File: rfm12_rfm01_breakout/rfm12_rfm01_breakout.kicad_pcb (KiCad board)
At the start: 2 copper layers, 32 x 24 mm, 13 parts, among them J1 ANT, J2 CONN_01X07, J3 INT, U1 RFM12B

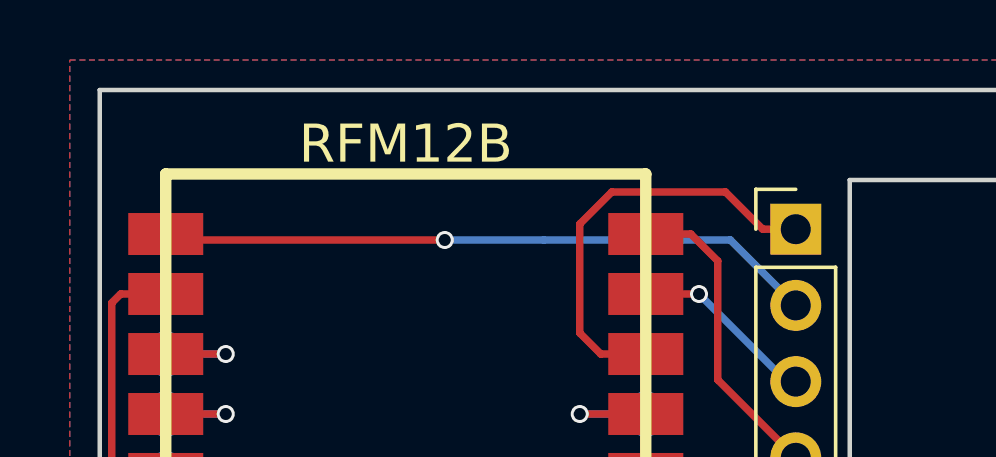
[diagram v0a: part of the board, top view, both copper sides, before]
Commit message: Minor silkscreen adjustments
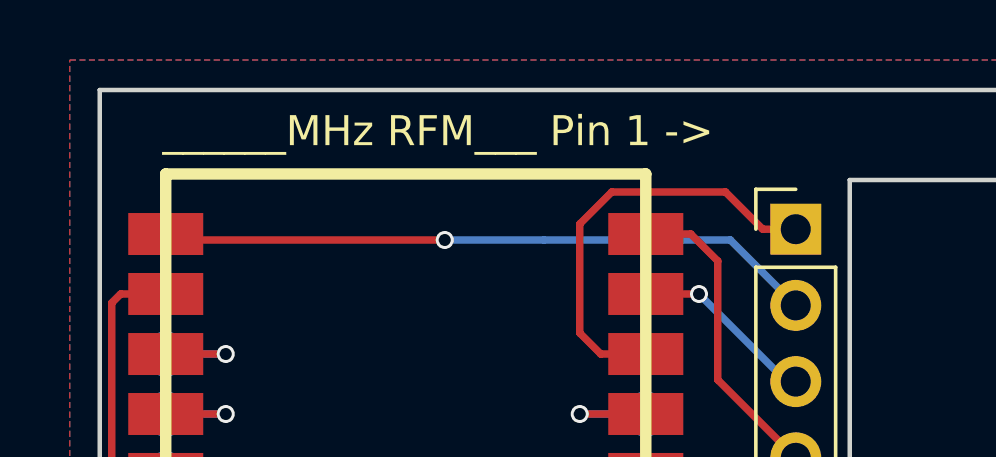
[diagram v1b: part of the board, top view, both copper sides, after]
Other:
- board text added: "For compatibility with using I2S boards at the same time, see manual in ZeroPhone Wiki"
- board text added: "RFM12/RFM01 mod board for ZeroPhone v1.0"
- board text added: "______MHz RFM___ Pin 1 ->"
- board text removed: "<- Pin 1"
- board text removed: "RFM12/RFM01 mod board for ZeroPhone For compatibility with using I2S boards at the same time, see manual in ZeroPhone Wiki"
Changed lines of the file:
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@@
-(kicad_pcb (version 4) (host pcbnew 4.0.6)
+(kicad_pcb (version 4) (host pcbnew 4.0.7)
   (general
     (links 22)
-    (no_connects 1)
+    (no_connects 0)
     (area 134.924999 98.924999 167.075001 123.075001)
     (thickness 1.6)
-    (drawings 8)
+    (drawings 9)
     (tracks 141)
     (zones 0)
@@
       (net 5 INT))
     (model ${KISYS3DMOD}/Pin_Headers.3dshapes/Pin_Header_Angled_1x07_Pitch2.54mm.wrl
-      (at (xyz 0 -0.3 0))
+      (at (xyz 0 0 0))
       (scale (xyz 1 1 1))
-      (rotate (xyz 0 0 90))
+      (rotate (xyz 0 0 0))
     )
   )
@@
       (effects (font (size 1 1) (thickness 0.15)) (justify mirror))
     )
-    (fp_text value FDF (at 1.6 0 90) (layer B.SilkS)
+    (fp_text value FDF (at -1.575 0 90) (layer B.SilkS)
       (effects (font (size 0.7 0.7) (thickness 0.15)) (justify mirror))
     )
@@
       (effects (font (size 1 1) (thickness 0.15)) (justify mirror))
     )
-    (fp_text value DCF (at -1.6 0 270) (layer B.SilkS)
+    (fp_text value DCF (at 1.525 -0.025 270) (layer B.SilkS)
       (effects (font (size 0.7 0.7) (thickness 0.15)) (justify mirror))
     )
@@
       (effects (font (size 1 1) (thickness 0.15)) (justify mirror))
     )
-    (fp_text value CK (at 1.6 0 270) (layer B.SilkS)
+    (fp_text value CK (at -1.55 0 270) (layer B.SilkS)
       (effects (font (size 0.7 0.7) (thickness 0.15)) (justify mirror))
     )
@@
       (effects (font (size 1 1) (thickness 0.15)) (justify mirror))
     )
-    (fp_text value RES (at 1.6 0 90) (layer B.SilkS)
+    (fp_text value RES (at -1.525 0 90) (layer B.SilkS)
       (effects (font (size 0.7 0.7) (thickness 0.15)) (justify mirror))
     )
@@
       (effects (font (thickness 0.3048)))
     )
-    (fp_text value RFM12B (at 0 -8.99922) (layer F.SilkS)
+    (fp_text value RFM12B (at 0 -8.99922) (layer F.SilkS) hide
       (effects (font (thickness 0.3048)))
     )
@@
       (net 5 INT))
   )
-  (gr_text "<- Pin 1\n" (at 153 102.5) (layer B.SilkS)
-    (effects (font (size 1 1) (thickness 0.25)) (justify mirror))
-  )
-  (gr_text "RFM12/RFM01\nmod board for\nZeroPhone\n\nFor compatibility\nwith using I2S \nboards at the same\ntime, see manual in\nZeroPhone Wiki" (at 145.5 112.5) (layer B.SilkS)
-    (effects (font (size 1 1) (thickness 0.25)) (justify mirror))
+  (gr_text "RFM12/RFM01\nmod board for\nZeroPhone\nv1.0" (at 145.75 105.25) (layer B.SilkS)
+    (effects (font (size 1.5 1.5) (thickness 0.3)) (justify mirror))
+  )
+  (gr_text "______MHz RFM___ Pin 1 ->\n" (at 146.275 100.375) (layer F.SilkS)
+    (effects (font (size 1 1) (thickness 0.2)))
+  )
+  (gr_text "For compatibility\nwith using I2S \nboards at the same\ntime, see manual in\nZeroPhone Wiki" (at 145.075 115.925) (layer B.SilkS)
+    (effects (font (size 1 1) (thickness 0.2)) (justify mirror))
   )
   (gr_line (start 135 123) (end 135 99) (layer Edge.Cuts) (width 0.15))
